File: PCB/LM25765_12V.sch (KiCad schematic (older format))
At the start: 8 parts

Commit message: Annotated Schematic
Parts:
- removed C57: 1uF, Capacitors:0603, symbol Device:C_Small
- removed C58: 0.1uF, Capacitors:0603, symbol Device:C_Small
- removed C?: 1000uF, Capacitor_SMD:CP_Elec_8x10, symbol Device:CP1_Small
- removed D?: B360AF, Diode_SMD:D_SMA, symbol Device:D_Schottky_Small
- removed L?: 100uH, Inductor_SMD:L_Wuerth_WE-PD-Typ-LS_Handsoldering, symbol Device:L_Small
- removed U?: LM2576S-12, Package_TO_SOT_SMD:TO-263-5_TabPin3, symbol Regulator_Switching:LM2576S-3.3
- added C29: 1000uF, Capacitor_SMD:CP_Elec_8x10, symbol Device:CP1_Small
- added C30: 1uF, Capacitors:0603, symbol Device:C_Small
- added C31: 0.1uF, Capacitors:0603, symbol Device:C_Small
- added D7: B360AF, Diode_SMD:D_SMA, symbol Device:D_Schottky_Small
- added L2: 100uH, Inductor_SMD:L_Wuerth_WE-PD-Typ-LS_Handsoldering, symbol Device:L_Small
- added U6: LM2576S-12, Package_TO_SOT_SMD:TO-263-5_TabPin3, symbol Regulator_Switching:LM2576S-3.3
- gave numbers to parts that had none: 1
- renumbered C59 to C32
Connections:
- net GND: now also C29.2, C30.2, C31.2, D7.2 (A), U6.3 (GND), U6.5 (~ON~/OFF)
- net Vin: now also U6.1 (VIN)
- net Vout: now also C29.1, C30.1, C31.1, L2.2, U6.4 (FB)
- new net: D7.1 (K), L2.1, U6.2 (OUT)

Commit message: Added Dielectric and voltage rating to all capacitors
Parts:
- C29, C32: Voltage Rating 6.3V -> 16V
- C30, C31: Voltage Rating (none) -> 16V
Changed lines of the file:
@@
 F 5 "Power Supply" H 6300 4050 50  0001 C CNN "Functional Block"
 F 6 "Aluminium Film" H -700 -100 50  0001 C CNN "Dielectric"
-F 7 "6.3V" H -700 -100 50  0001 C CNN "Voltage Rating"
+F 7 "16V" H -700 -100 50  0001 C CNN "Voltage Rating"
 F 8 "General Purpose" H -700 -100 50  0001 C CNN "Impedance"
 F 9 "1000hr @ 85degC" H -700 -100 50  0001 C CNN "Lifetime @ Temperature"
@@
 F 4 "Power Supply" H 6800 4050 50  0001 C CNN "Functional Block"
 F 5 "X7R" H -700 -100 50  0001 C CNN "Dielectric"
+F 6 "16V" H 6800 4050 50  0001 C CNN "Voltage Rating"
 	1    6800 4050
 	1    0    0    -1
@@
 F 4 "Power Supply" H 7150 4050 50  0001 C CNN "Functional Block"
 F 5 "X7R" H -700 -100 50  0001 C CNN "Dielectric"
+F 6 "16V" H 7150 4050 50  0001 C CNN "Voltage Rating"
 	1    7150 4050
 	1    0    0    -1
@@
 F 6 "Power Supply" H 7550 4050 50  0001 C CNN "Functional Block"
 F 7 "Aluminium Film" H -700 -100 50  0001 C CNN "Dielectric"
-F 8 "6.3V" H -700 -100 50  0001 C CNN "Voltage Rating"
+F 8 "16V" H -700 -100 50  0001 C CNN "Voltage Rating"
 F 9 "General Purpose" H -700 -100 50  0001 C CNN "Impedance"
 F 10 "1000hr @ 85degC" H -700 -100 50  0001 C CNN "Lifetime @ Temperature"

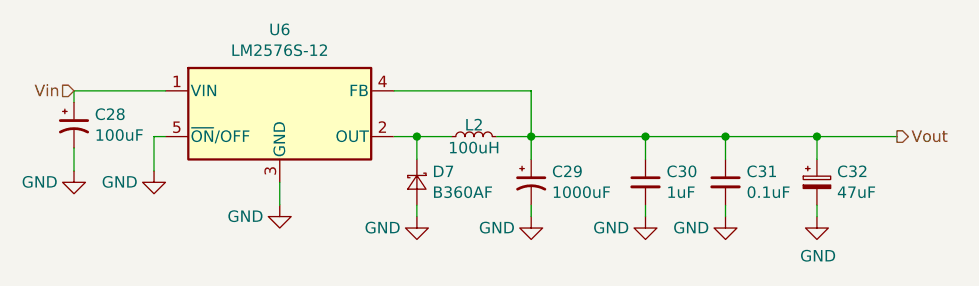
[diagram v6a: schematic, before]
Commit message: Added Humidity and temperature sensors
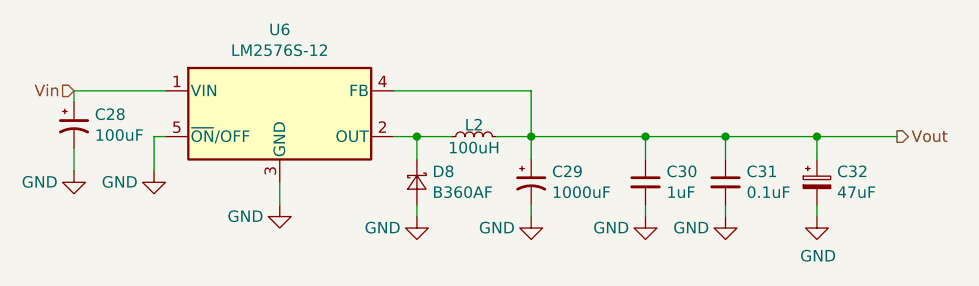
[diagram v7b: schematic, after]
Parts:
- renumbered D7 to D8
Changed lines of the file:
@@
 AR Path="/5E880E11/5E904307/5E8CA262" Ref="#PWR?"  Part="1"
 AR Path="/5E880E11/5E9C764B/5E8CA262" Ref="#PWR?"  Part="1"
-AR Path="/5E880E11/5E9C98F5/5E8CA262" Ref="#PWR082"  Part="1"
-F 0 "#PWR082" H 5200 3900 50  0001 C CNN
+AR Path="/5E880E11/5E9C98F5/5E8CA262" Ref="#PWR085"  Part="1"
+F 0 "#PWR085" H 5200 3900 50  0001 C CNN
 F 1 "GND" H 5050 4100 50  0000 C CNN
 F 2 "" H 5200 4150 50  0001 C CNN
@@
 AR Path="/5E880E11/5E904307/5E8CA265" Ref="#PWR?"  Part="1"
 AR Path="/5E880E11/5E9C764B/5E8CA265" Ref="#PWR?"  Part="1"
-AR Path="/5E880E11/5E9C98F5/5E8CA265" Ref="#PWR084"  Part="1"
-F 0 "#PWR084" H 6300 3950 50  0001 C CNN
+AR Path="/5E880E11/5E9C98F5/5E8CA265" Ref="#PWR087"  Part="1"
+F 0 "#PWR087" H 6300 3950 50  0001 C CNN
 F 1 "GND" H 6150 4150 50  0000 C CNN
 F 2 "" H 6300 4200 50  0001 C CNN
@@
 AR Path="/5E880E11/5E904307/5E8CA267" Ref="#PWR?"  Part="1"
 AR Path="/5E880E11/5E9C764B/5E8CA267" Ref="#PWR?"  Part="1"
-AR Path="/5E880E11/5E9C98F5/5E8CA267" Ref="#PWR083"  Part="1"
-F 0 "#PWR083" H 5800 3950 50  0001 C CNN
+AR Path="/5E880E11/5E9C98F5/5E8CA267" Ref="#PWR086"  Part="1"
+F 0 "#PWR086" H 5800 3950 50  0001 C CNN
 F 1 "GND" H 5650 4150 50  0000 C CNN
 F 2 "" H 5800 4200 50  0001 C CNN
@@
 AR Path="/5E880E11/5E904307/5E8CA26B" Ref="D?"  Part="1"
 AR Path="/5E880E11/5E9C764B/5E8CA26B" Ref="D?"  Part="1"
-AR Path="/5E880E11/5E9C98F5/5E8CA26B" Ref="D7"  Part="1"
-F 0 "D7" V 5754 4118 50  0000 L CNN
+AR Path="/5E880E11/5E9C98F5/5E8CA26B" Ref="D8"  Part="1"
+F 0 "D8" V 5754 4118 50  0000 L CNN
 F 1 "B360AF" V 5845 4118 50  0000 L CNN
 F 2 "Diode_SMD:D_SMA" V 5800 4050 50  0001 C CNN
@@
 AR Path="/5E880E11/5E904307/5B9CEE03" Ref="#PWR?"  Part="1"
 AR Path="/5E880E11/5E9C764B/5B9CEE03" Ref="#PWR?"  Part="1"
-AR Path="/5E880E11/5E9C98F5/5B9CEE03" Ref="#PWR087"  Part="1"
-F 0 "#PWR087" H 7550 3950 50  0001 C CNN
+AR Path="/5E880E11/5E9C98F5/5B9CEE03" Ref="#PWR090"  Part="1"
+F 0 "#PWR090" H 7550 3950 50  0001 C CNN
 F 1 "GND" H 7555 4027 50  0000 C CNN
 F 2 "" H 7550 4200 50  0001 C CNN
@@
 AR Path="/5E880E11/5E904307/5B9D0690" Ref="#PWR?"  Part="1"
 AR Path="/5E880E11/5E9C764B/5B9D0690" Ref="#PWR?"  Part="1"
-AR Path="/5E880E11/5E9C98F5/5B9D0690" Ref="#PWR085"  Part="1"
-F 0 "#PWR085" H 6800 3950 50  0001 C CNN
+AR Path="/5E880E11/5E9C98F5/5B9D0690" Ref="#PWR088"  Part="1"
+F 0 "#PWR088" H 6800 3950 50  0001 C CNN
 F 1 "GND" H 6650 4150 50  0000 C CNN
 F 2 "" H 6800 4200 50  0001 C CNN
@@
 AR Path="/5E880E11/5E904307/5B9D06AF" Ref="#PWR?"  Part="1"
 AR Path="/5E880E11/5E9C764B/5B9D06AF" Ref="#PWR?"  Part="1"
-AR Path="/5E880E11/5E9C98F5/5B9D06AF" Ref="#PWR086"  Part="1"
-F 0 "#PWR086" H 7150 3950 50  0001 C CNN
+AR Path="/5E880E11/5E9C98F5/5B9D06AF" Ref="#PWR089"  Part="1"
+F 0 "#PWR089" H 7150 3950 50  0001 C CNN
 F 1 "GND" H 7000 4150 50  0000 C CNN
 F 2 "" H 7150 4200 50  0001 C CNN
@@
 AR Path="/5E880E11/5E904307/5B713FC7" Ref="#PWR?"  Part="1"
 AR Path="/5E880E11/5E9C764B/5B713FC7" Ref="#PWR?"  Part="1"
-AR Path="/5E880E11/5E9C98F5/5B713FC7" Ref="#PWR081"  Part="1"
-F 0 "#PWR081" H 4650 3750 50  0001 C CNN
+AR Path="/5E880E11/5E9C98F5/5B713FC7" Ref="#PWR084"  Part="1"
+F 0 "#PWR084" H 4650 3750 50  0001 C CNN
 F 1 "GND" H 4500 3950 50  0000 C CNN
 F 2 "" H 4650 4000 50  0001 C CNN
@@
 AR Path="/5E880E11/5E904307/5B713FD6" Ref="#PWR?"  Part="1"
 AR Path="/5E880E11/5E9C764B/5B713FD6" Ref="#PWR?"  Part="1"
-AR Path="/5E880E11/5E9C98F5/5B713FD6" Ref="#PWR080"  Part="1"
-F 0 "#PWR080" H 4300 3750 50  0001 C CNN
+AR Path="/5E880E11/5E9C98F5/5B713FD6" Ref="#PWR083"  Part="1"
+F 0 "#PWR083" H 4300 3750 50  0001 C CNN
 F 1 "GND" H 4150 3950 50  0000 C CNN
 F 2 "" H 4300 4000 50  0001 C CNN
